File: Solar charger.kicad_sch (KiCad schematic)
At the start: 12 parts, among them J1 SOLAR_IN, J2 BATTERY, J3 POWER_OUT, J4 BAT_MON, U1 MCP1700x-330xxTO, U2 TP4056

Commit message: Replace micro JSTs with terminal blocks (#3)
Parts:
- J1, J2, J3, J4: footprint Connector_Molex:Molex_PicoBlade_53047-0210_1x02_P1.25mm_Vertical -> TerminalBlock_Phoenix:TerminalBlock_Phoenix_MKDS-1,5-2-5.08_1x02_P5.08mm_Horizontal
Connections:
- net BAT_GND: now also J2.1 (Pin_1); no longer J2.2 (Pin_2)
- net BAT_IN: now also J2.2 (Pin_2); no longer J2.1 (Pin_1)
- net SOLAR_GND: now also J1.2 (Pin_2); no longer J1.1 (Pin_1)
- net SOLAR_IN: now also J1.1 (Pin_1); no longer J1.2 (Pin_2)
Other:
- moved on the sheet: J1, J2
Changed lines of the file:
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@@
 	(wire
 		(pts
-			(xy 161.29 119.38) (xy 157.48 119.38)
+			(xy 157.48 119.38) (xy 168.91 119.38)
 		)
 		(stroke
@@
 	(wire
 		(pts
+			(xy 134.62 120.65) (xy 134.62 118.11)
+		)
+		(stroke
+			(width 0)
+			(type default)
+		)
+	)
+	(wire
+		(pts
 			(xy 92.71 110.49) (xy 92.71 114.3)
 		)
@@
 	(wire
 		(pts
+			(xy 125.73 125.73) (xy 125.73 123.19)
+		)
+		(stroke
+			(width 0)
+			(type default)
+		)
+	)
+	(wire
+		(pts
 			(xy 92.71 110.49) (xy 101.6 110.49)
 		)
@@
 	(wire
 		(pts
-			(xy 157.48 124.46) (xy 161.29 124.46)
+			(xy 157.48 124.46) (xy 168.91 124.46)
+		)
+		(stroke
+			(width 0)
+			(type default)
+		)
+	)
+	(wire
+		(pts
+			(xy 168.91 124.46) (xy 168.91 123.19)
 		)
 		(stroke
@@
 	(wire
 		(pts
+			(xy 125.73 118.11) (xy 125.73 120.65)
+		)
+		(stroke
+			(width 0)
+			(type default)
+		)
+	)
+	(wire
+		(pts
+			(xy 134.62 123.19) (xy 134.62 125.73)
+		)
+		(stroke
+			(width 0)
+			(type default)
+		)
+	)
+	(wire
+		(pts
 			(xy 139.7 110.49) (xy 139.7 119.38)
 		)
@@
 	(wire
 		(pts
+			(xy 134.62 125.73) (xy 125.73 125.73)
+		)
+		(stroke
+			(width 0)
+			(type default)
+		)
+	)
+	(wire
+		(pts
 			(xy 134.62 120.65) (xy 139.7 120.65)
 		)
@@
 	(wire
 		(pts
+			(xy 168.91 119.38) (xy 168.91 120.65)
+		)
+		(stroke
+			(width 0)
+			(type default)
+		)
+	)
+	(wire
+		(pts
 			(xy 115.57 118.11) (xy 109.22 118.11)
 		)
@@
 	(wire
 		(pts
-			(xy 161.29 123.19) (xy 161.29 124.46)
+			(xy 134.62 118.11) (xy 125.73 118.11)
 		)
 		(stroke
@@
 		(pts
 			(xy 82.55 114.3) (xy 82.55 110.49)
-		)
-		(stroke
-			(width 0)
-			(type default)
-		)
-	)
-	(wire
-		(pts
-			(xy 161.29 120.65) (xy 161.29 119.38)
 		)
 		(stroke
@@
 			)
 		)
-		(property "Footprint" "Connector_Molex:Molex_PicoBlade_53047-0210_1x02_P1.25mm_Vertical"
+		(property "Footprint" "TerminalBlock_Phoenix:TerminalBlock_Phoenix_MKDS-1,5-2-5.08_1x02_P5.08mm_Horizontal"
 			(at 134.62 143.51 0)
 			(hide yes)
@@
 	(symbol
 		(lib_id "Connector_Generic:Conn_01x02")
-		(at 129.54 123.19 180)
+		(at 130.81 120.65 0)
 		(unit 1)
 		(body_style 1)
@@
 		(dnp no)
 		(property "Reference" "J2"
-			(at 129.54 114.3 0)
+			(at 130.81 129.54 0)
 			(show_name no)
 			(do_not_autoplace no)
@@
 		)
 		(property "Value" "BATTERY"
-			(at 129.54 116.84 0)
-			(show_name no)
-			(do_not_autoplace no)
-			(effects
-				(font
-					(size 1.27 1.27)
-				)
-			)
-		)
-		(property "Footprint" "Connector_Molex:Molex_PicoBlade_53047-0210_1x02_P1.25mm_Vertical"
-			(at 129.54 123.19 0)
+			(at 130.81 127 0)
+			(show_name no)
+			(do_not_autoplace no)
+			(effects
+				(font
+					(size 1.27 1.27)
+				)
+			)
+		)
+		(property "Footprint" "TerminalBlock_Phoenix:TerminalBlock_Phoenix_MKDS-1,5-2-5.08_1x02_P5.08mm_Horizontal"
+			(at 130.81 120.65 0)
 			(hide yes)
 			(show_name no)
@@
 		)
 		(property "Datasheet" ""
-			(at 129.54 123.19 0)
+			(at 130.81 120.65 0)
 			(hide yes)
 			(show_name no)
@@
 		)
 		(property "Description" "Generic connector, single row, 01x02, script generated (kicad-library-utils/schlib/autogen/connector/)"
-			(at 129.54 123.19 0)
+			(at 130.81 120.65 0)
 			(hide yes)
 			(show_name no)
@@
 			)
 		)
-		(property "Footprint" "Connector_Molex:Molex_PicoBlade_53047-0210_1x02_P1.25mm_Vertical"
+		(property "Footprint" "TerminalBlock_Phoenix:TerminalBlock_Phoenix_MKDS-1,5-2-5.08_1x02_P5.08mm_Horizontal"
 			(at 101.6 95.25 0)
 			(hide yes)
@@
 	(symbol
 		(lib_id "Connector_Generic:Conn_01x02")
-		(at 166.37 120.65 0)
+		(at 163.83 123.19 180)
 		(unit 1)
 		(body_style 1)
@@
 		(dnp no)
 		(property "Reference" "J1"
-			(at 166.37 132.08 0)
+			(at 163.83 111.76 0)
 			(show_name no)
 			(do_not_autoplace no)
@@
 		)
 		(property "Value" "SOLAR_IN"
-			(at 165.1 127 0)
-			(show_name no)
-			(do_not_autoplace no)
-			(effects
-				(font
-					(size 1.27 1.27)
-				)
-			)
-		)
-		(property "Footprint" "Connector_Molex:Molex_PicoBlade_53047-0210_1x02_P1.25mm_Vertical"
-			(at 166.37 120.65 0)
+			(at 165.1 116.84 0)
+			(show_name no)
+			(do_not_autoplace no)
+			(effects
+				(font
+					(size 1.27 1.27)
+				)
+			)
+		)
+		(property "Footprint" "TerminalBlock_Phoenix:TerminalBlock_Phoenix_MKDS-1,5-2-5.08_1x02_P5.08mm_Horizontal"
+			(at 163.83 123.19 0)
 			(hide yes)
 			(show_name no)
@@
 		)
 		(property "Datasheet" ""
-			(at 166.37 120.65 0)
+			(at 163.83 123.19 0)
 			(hide yes)
 			(show_name no)
@@
 		)
 		(property "Description" "Generic connector, single row, 01x02, script generated (kicad-library-utils/schlib/autogen/connector/)"
-			(at 166.37 120.65 0)
-			(hide yes)
-			(show_name no)
+			(at 163.83 123.19 0)
+			(hide yes)
+			(show_name no)

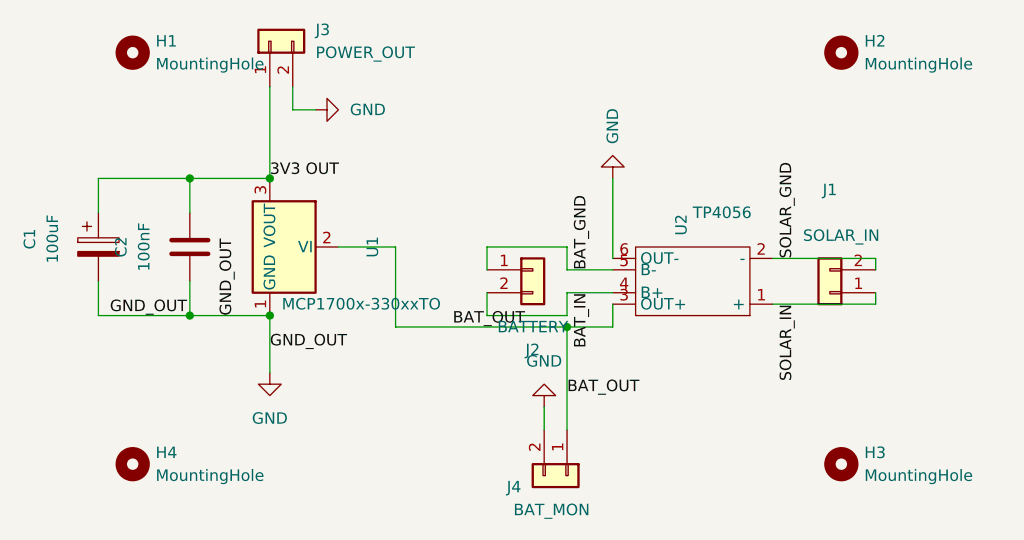
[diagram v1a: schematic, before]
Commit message: Fix TP4056 pads spacing, replace volatge regulator, tweaks (#5)
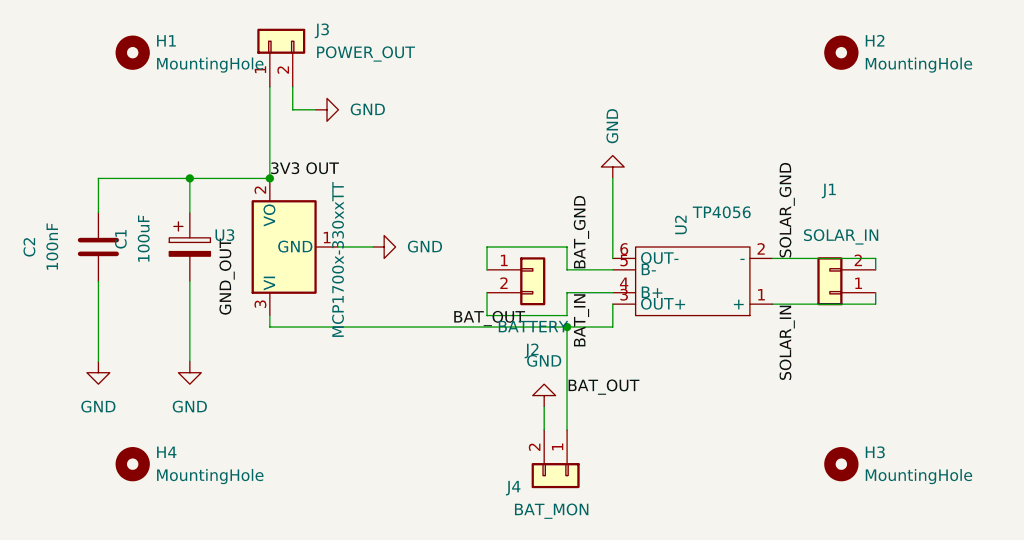
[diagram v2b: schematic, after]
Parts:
- removed U1: MCP1700x-330xxTO, Package_TO_SOT_THT:TO-92_Inline, symbol Regulator_Linear:MCP1700x-330xxTO
- added U3: MCP1700x-330xxTT, Package_TO_SOT_SMD:SOT-23_Handsoldering, symbol Regulator_Linear:MCP1700x-330xxTT
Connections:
- net 3V3 OUT: now also U3.2 (VO)
- net BAT_OUT: now also U3.3 (VI)
- net GND: now also U3.1 (GND)
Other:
- moved on the sheet: C1, C2
